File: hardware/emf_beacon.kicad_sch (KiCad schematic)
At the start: 4 parts

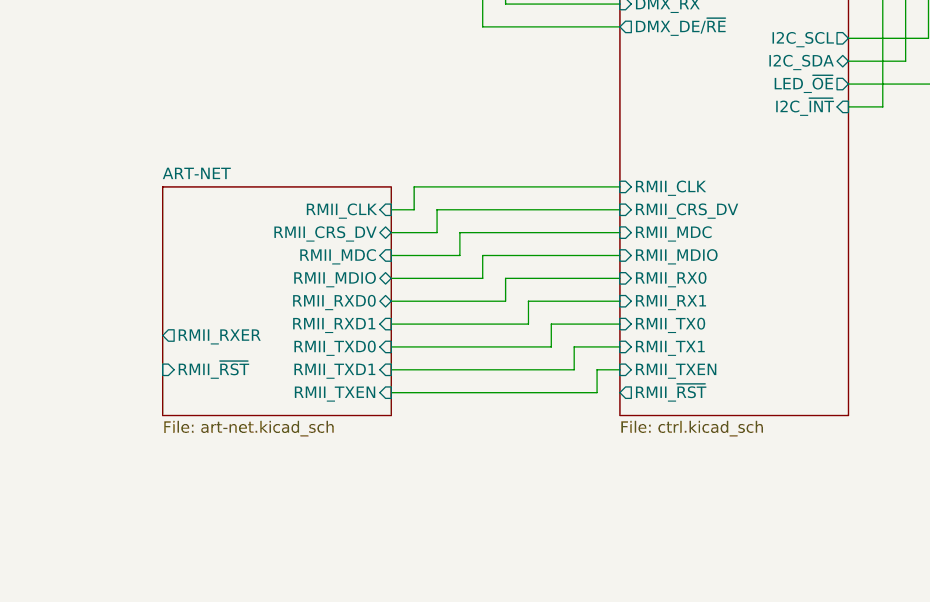
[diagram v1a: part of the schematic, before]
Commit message: removed Art-Net
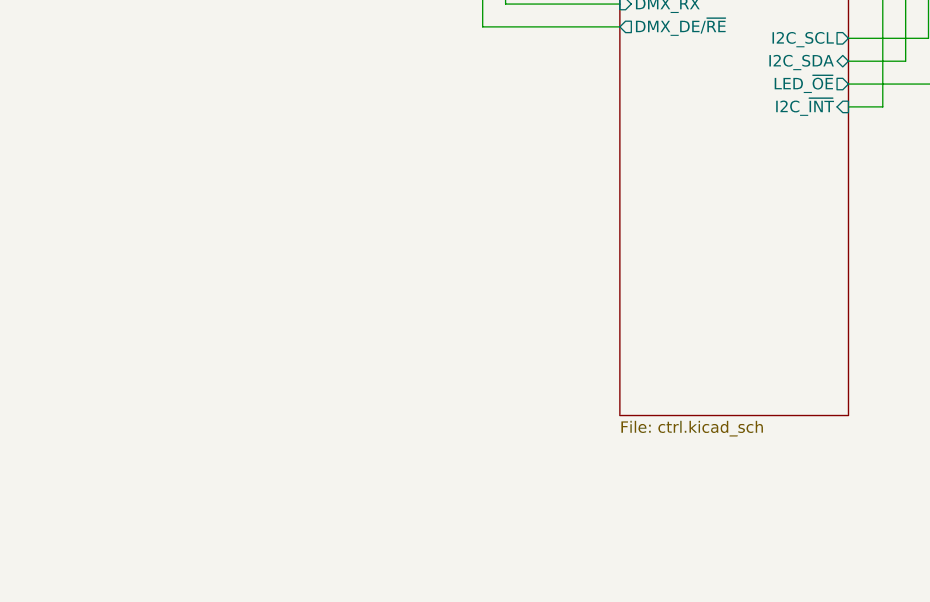
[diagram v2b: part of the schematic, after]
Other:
- removed sheet ART-NET
- sheet CTRL ports: added none; removed RMII_CLK, RMII_CRS_DV, RMII_MDC, RMII_MDIO, RMII_RX0, RMII_RX1, RMII_TX0, RMII_TX1, RMII_TXEN, RMII_~{RST}

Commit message: clean up
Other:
- note added: "LED Beacon"
- note removed: "DMX512's XLRs and Art-Net's RJ45 may get spun out to external PCBs"
- note removed: "Spec: Interfaces: Ideally DMX512 (5pin XLR) and Art-Net (RJ45) At least one, slight DMX512 preference +12V DC input weatherproof connections 10x 6.4V 0.3A LED strips Control: Treat as 10x lights per beacon be able to set normal brightness for each 'light' but fast enough for strobe effect for each 'light' Misc: JLC Assembly Target quantity is 15"

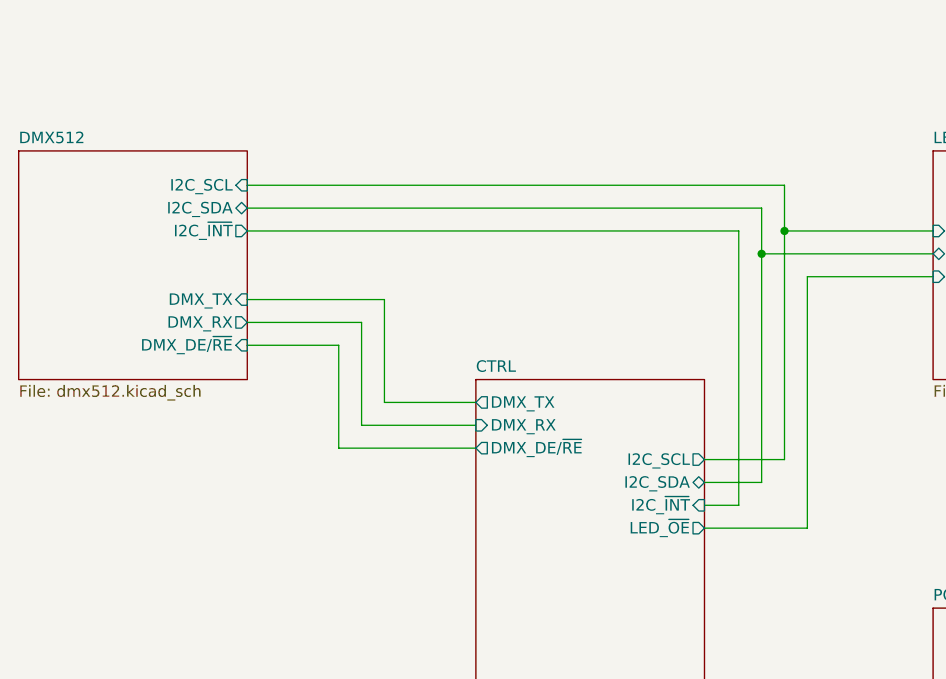
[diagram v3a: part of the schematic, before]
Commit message: adding snubbers, starting placement
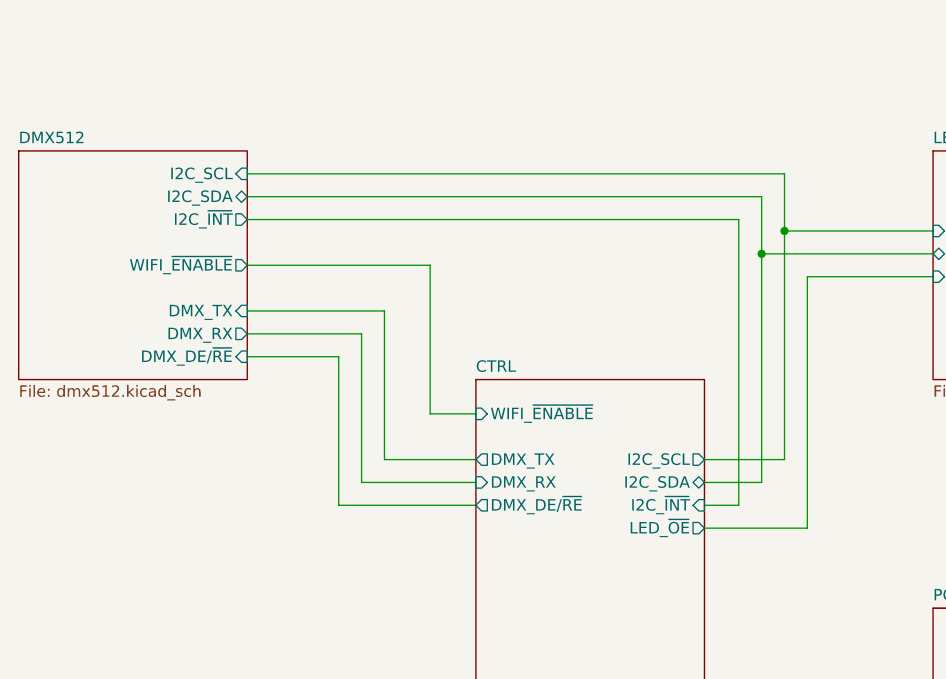
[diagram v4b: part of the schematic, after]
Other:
- sheet CTRL ports: added WIFI_~{ENABLE}; removed none
- sheet DMX512 ports: added WIFI_~{ENABLE}; removed none
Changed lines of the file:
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@@
 	(wire
 		(pts
-			(xy 116.84 78.74) (xy 127 78.74)
-		)
-		(stroke
-			(width 0)
-			(type default)
-		)
-	)
-	(wire
-		(pts
-			(xy 101.6 59.69) (xy 156.21 59.69)
-		)
-		(stroke
-			(width 0)
-			(type default)
-		)
-	)
-	(wire
-		(pts
-			(xy 156.21 59.69) (xy 156.21 90.17)
-		)
-		(stroke
-			(width 0)
-			(type default)
-		)
-	)
-	(wire
-		(pts
-			(xy 101.6 72.39) (xy 111.76 72.39)
-		)
-		(stroke
-			(width 0)
-			(type default)
-		)
-	)
-	(wire
-		(pts
-			(xy 101.6 57.15) (xy 158.75 57.15)
-		)
-		(stroke
-			(width 0)
-			(type default)
-		)
-	)
-	(wire
-		(pts
-			(xy 101.6 54.61) (xy 161.29 54.61)
+			(xy 116.84 85.09) (xy 127 85.09)
+		)
+		(stroke
+			(width 0)
+			(type default)
+		)
+	)
+	(wire
+		(pts
+			(xy 101.6 58.42) (xy 156.21 58.42)
+		)
+		(stroke
+			(width 0)
+			(type default)
+		)
+	)
+	(wire
+		(pts
+			(xy 156.21 58.42) (xy 156.21 90.17)
+		)
+		(stroke
+			(width 0)
+			(type default)
+		)
+	)
+	(wire
+		(pts
+			(xy 101.6 73.66) (xy 111.76 73.66)
+		)
+		(stroke
+			(width 0)
+			(type default)
+		)
+	)
+	(wire
+		(pts
+			(xy 101.6 55.88) (xy 158.75 55.88)
+		)
+		(stroke
+			(width 0)
+			(type default)
+		)
+	)
+	(wire
+		(pts
+			(xy 101.6 53.34) (xy 161.29 53.34)
 		)
 		(stroke
@@
 	(wire
 		(pts
-			(xy 127 81.28) (xy 114.3 81.28)
-		)
-		(stroke
-			(width 0)
-			(type default)
-		)
-	)
-	(wire
-		(pts
-			(xy 161.29 54.61) (xy 161.29 59.69)
+			(xy 127 87.63) (xy 114.3 87.63)
+		)
+		(stroke
+			(width 0)
+			(type default)
+		)
+	)
+	(wire
+		(pts
+			(xy 161.29 53.34) (xy 161.29 59.69)
+		)
+		(stroke
+			(width 0)
+			(type default)
+		)
+	)
+	(wire
+		(pts
+			(xy 121.92 63.5) (xy 101.6 63.5)
 		)
 		(stroke
@@
 	(wire
 		(pts
-			(xy 111.76 72.39) (xy 111.76 83.82)
+			(xy 111.76 73.66) (xy 111.76 90.17)
 		)
 		(stroke
@@
 	(wire
 		(pts
-			(xy 114.3 81.28) (xy 114.3 69.85)
+			(xy 114.3 87.63) (xy 114.3 71.12)
 		)
 		(stroke
@@
 	(wire
 		(pts
-			(xy 116.84 67.31) (xy 116.84 78.74)
+			(xy 121.92 80.01) (xy 121.92 63.5)
+		)
+		(stroke
+			(width 0)
+			(type default)
+		)
+	)
+	(wire
+		(pts
+			(xy 116.84 68.58) (xy 116.84 85.09)
 		)
 		(stroke
@@
 	(wire
 		(pts
-			(xy 158.75 57.15) (xy 158.75 62.23)
+			(xy 158.75 55.88) (xy 158.75 62.23)
 		)
 		(stroke
@@
 	(wire
 		(pts
-			(xy 111.76 83.82) (xy 127 83.82)
-		)
-		(stroke
-			(width 0)
-			(type default)
-		)
-	)
-	(wire
-		(pts
-			(xy 114.3 69.85) (xy 101.6 69.85)
-		)
-		(stroke
-			(width 0)
-			(type default)
-		)
-	)
-	(wire
-		(pts
-			(xy 101.6 67.31) (xy 116.84 67.31)
+			(xy 127 80.01) (xy 121.92 80.01)
+		)
+		(stroke
+			(width 0)
+			(type default)
+		)
+	)
+	(wire
+		(pts
+			(xy 111.76 90.17) (xy 127 90.17)
+		)
+		(stroke
+			(width 0)
+			(type default)
+		)
+	)
+	(wire
+		(pts
+			(xy 114.3 71.12) (xy 101.6 71.12)
+		)
+		(stroke
+			(width 0)
+			(type default)
+		)
+	)
+	(wire
+		(pts
+			(xy 101.6 68.58) (xy 116.84 68.58)
 		)
 		(stroke
@@
 		)
 		(pin "DMX_DE{slash}~{RE}" output
-			(at 127 83.82 180)
+			(at 127 90.17 180)
 			(effects
 				(font
@@
 		)
 		(pin "DMX_RX" input
-			(at 127 81.28 180)
+			(at 127 87.63 180)
 			(effects
 				(font
@@
 		)
 		(pin "DMX_TX" output
-			(at 127 78.74 180)
+			(at 127 85.09 180)
 			(effects
 				(font
@@
 				)
 				(justify right)
+			)
+		)
+		(pin "WIFI_~{ENABLE}" input
+			(at 127 80.01 180)
+			(effects
+				(font
+					(size 1.27 1.27)
+				)
+				(justify left)
 			)
 		)
@@
 		)
 		(pin "DMX_DE{slash}~{RE}" input
-			(at 101.6 72.39 0)
+			(at 101.6 73.66 0)
 			(effects
 				(font
@@
 		)
 		(pin "DMX_RX" output
-			(at 101.6 69.85 0)
+			(at 101.6 71.12 0)
 			(effects
 				(font
@@
 		)
 		(pin "DMX_TX" input
-			(at 101.6 67.31 0)
+			(at 101.6 68.58 0)
 			(effects
 				(font
@@
 		)
 		(pin "I2C_SDA" bidirectional
-			(at 101.6 57.15 0)
+			(at 101.6 55.88 0)
 			(effects
 				(font
@@
 		)
 		(pin "I2C_~{INT}" output
-			(at 101.6 59.69 0)
+			(at 101.6 58.42 0)
 			(effects
 				(font
@@
 		)
 		(pin "I2C_SCL" input
-			(at 101.6 54.61 0)
-			(effects
-				(font
+			(at 101.6 53.34 0)
+			(effects
+				(font
+					(size 1.27 1.27)
+				)
+				(justify right)
+			)
+		)
+		(pin "WIFI_~{ENABLE}" output
+			(at 101.6 63.5 0)
+			(effects
+				(font

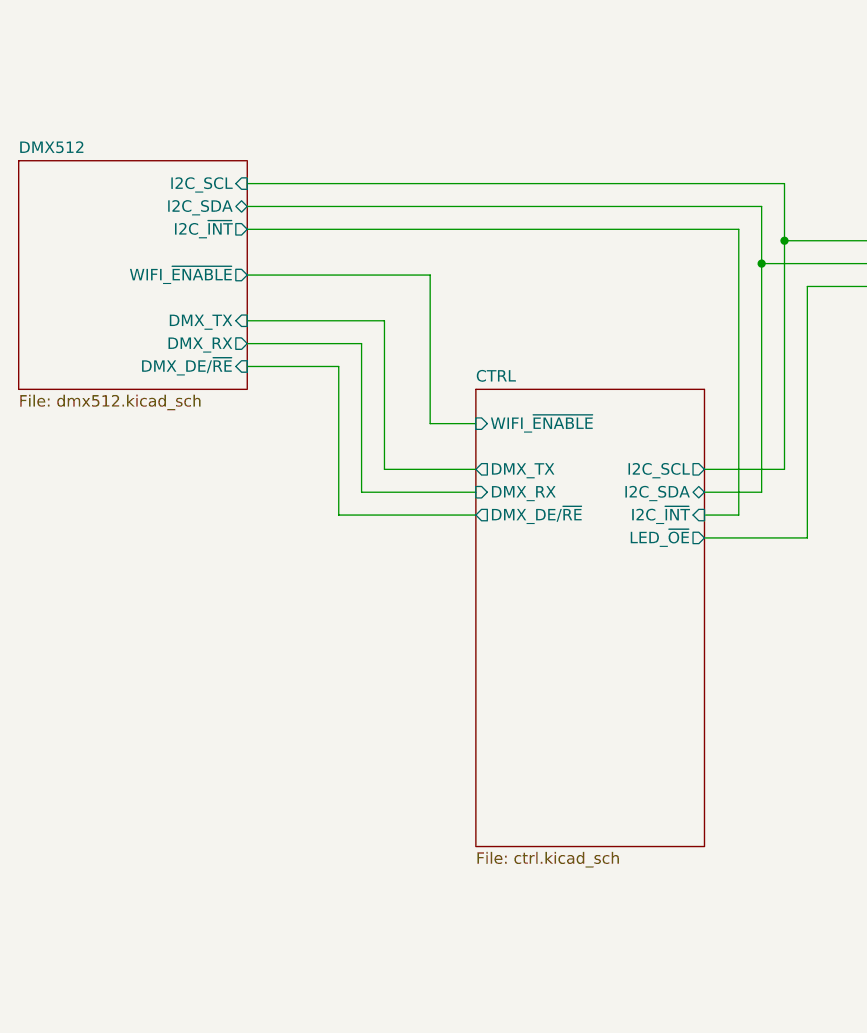
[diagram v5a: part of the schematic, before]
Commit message: sorting button and LED
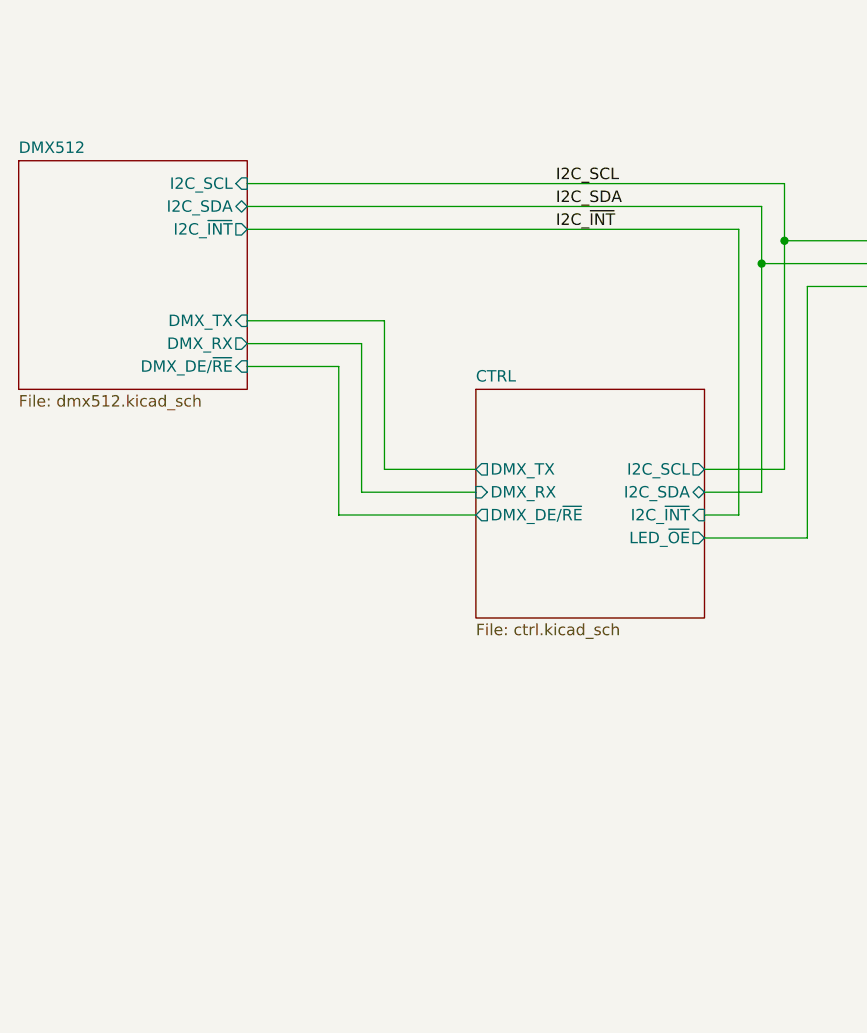
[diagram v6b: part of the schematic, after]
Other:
- sheet CTRL ports: added none; removed WIFI_~{ENABLE}
- sheet DMX512 ports: added none; removed WIFI_~{ENABLE}
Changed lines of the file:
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@@
-	(wire
-		(pts
-			(xy 121.92 63.5) (xy 101.6 63.5)
-		)
-		(stroke
-			(width 0)
-			(type default)
-		)
-	)
 	(wire
 		(pts
@@
 	(wire
 		(pts
-			(xy 121.92 80.01) (xy 121.92 63.5)
-		)
-		(stroke
-			(width 0)
-			(type default)
-		)
-	)
-	(wire
-		(pts
 			(xy 116.84 68.58) (xy 116.84 85.09)
 		)
@@
 	(wire
 		(pts
-			(xy 127 80.01) (xy 121.92 80.01)
-		)
-		(stroke
-			(width 0)
-			(type default)
-		)
-	)
-	(wire
-		(pts
 			(xy 111.76 90.17) (xy 127 90.17)
 		)
@@
 			(width 0)
 			(type default)
+		)
+	)
+	(label "I2C_~{INT}"
+		(at 135.89 58.42 0)
+		(effects
+			(font
+				(size 1.27 1.27)
+			)
+			(justify left bottom)
+		)
+	)
+	(label "I2C_SCL"
+		(at 135.89 53.34 0)
+		(effects
+			(font
+				(size 1.27 1.27)
+			)
+			(justify left bottom)
+		)
+	)
+	(label "I2C_SDA"
+		(at 135.89 55.88 0)
+		(effects
+			(font
+				(size 1.27 1.27)
+			)
+			(justify left bottom)
 		)
 	)
@@
 			)
 		)
-		(property "Rotation_offset" ""
-			(at 172.72 184.15 0)
-			(effects
-				(font
-					(size 1.27 1.27)
-				)
-				(hide yes)
-			)
-		)
 		(instances
 			(project "home_emf_beacon"
@@
 			)
 		)
-		(property "Rotation_offset" ""
-			(at 172.72 171.45 0)
-			(effects
-				(font
-					(size 1.27 1.27)
-				)
-				(hide yes)
-			)
-		)
 		(instances
 			(project ""
@@
 			)
 		)
-		(property "Rotation_offset" ""
-			(at 172.72 177.8 0)
-			(effects
-				(font
-					(size 1.27 1.27)
-				)
-				(hide yes)
-			)
-		)
 		(instances
 			(project "home_emf_beacon"
@@
 			)
 		)
-		(property "Rotation_offset" ""
-			(at 172.72 190.5 0)
-			(effects
-				(font
-					(size 1.27 1.27)
-				)
-				(hide yes)
-			)
-		)
 		(instances
 			(project "home_emf_beacon"
@@
 	(sheet
 		(at 127 76.2)
-		(size 25.4 50.8)
+		(size 25.4 25.4)
 		(exclude_from_sim no)
 		(in_bom yes)
@@
 		)
 		(property "Sheetfile" "ctrl.kicad_sch"
-			(at 127 127.5846 0)
+			(at 127 102.1846 0)
 			(effects
 				(font
@@
 				)
 				(justify right)
-			)
-		)
-		(pin "WIFI_~{ENABLE}" input
-			(at 127 80.01 180)
-			(effects
-				(font
-					(size 1.27 1.27)
-				)
-				(justify left)
 			)
 		)
@@
 			(effects
 				(font
-					(size 1.27 1.27)
-				)
-				(justify right)
-			)
-		)
-		(pin "WIFI_~{ENABLE}" output
-			(at 101.6 63.5 0)
-			(effects
-				(font

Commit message: starting layout
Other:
- sheet CTRL ports: added LED_~{PGD}; removed none
- sheet POWER ports: added LED_~{PGD}; removed none
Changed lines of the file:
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@@
+	(wire
+		(pts
+			(xy 163.83 114.3) (xy 163.83 95.25)
+		)
+		(stroke
+			(width 0)
+			(type default)
+		)
+	)
 	(wire
 		(pts
@@
 	(wire
 		(pts
+			(xy 177.8 114.3) (xy 163.83 114.3)
+		)
+		(stroke
+			(width 0)
+			(type default)
+		)
+	)
+	(wire
+		(pts
 			(xy 156.21 58.42) (xy 156.21 90.17)
 		)
@@
 		(pts
 			(xy 152.4 90.17) (xy 156.21 90.17)
+		)
+		(stroke
+			(width 0)
+			(type default)
+		)
+	)
+	(wire
+		(pts
+			(xy 152.4 95.25) (xy 163.83 95.25)
 		)
 		(stroke
@@
 			)
 		)
+		(pin "LED_~{PGD}" output
+			(at 177.8 114.3 180)
+			(effects
+				(font
+					(size 1.27 1.27)
+				)
+				(justify left)
+			)
+		)
 		(instances
 			(project "emf_beacon"
@@
 			(effects
 				(font
+					(size 1.27 1.27)
+				)
+				(justify right)
+			)
+		)
+		(pin "LED_~{PGD}" input
+			(at 152.4 95.25 0)
+			(effects
+				(font

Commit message: more layout and fixing OOS items
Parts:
- H1, H2, H3, H4: symbol Mechanical:MountingHole -> emf_beacon_ibrary:MountingHole
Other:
- sheet CTRL ports: added none; removed LED_~{PGD}
- sheet POWER ports: added none; removed LED_~{PGD}
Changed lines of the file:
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@@
-	(wire
-		(pts
-			(xy 163.83 114.3) (xy 163.83 95.25)
-		)
-		(stroke
-			(width 0)
-			(type default)
-		)
-	)
 	(wire
 		(pts
@@
 	(wire
 		(pts
-			(xy 177.8 114.3) (xy 163.83 114.3)
-		)
-		(stroke
-			(width 0)
-			(type default)
-		)
-	)
-	(wire
-		(pts
 			(xy 156.21 58.42) (xy 156.21 90.17)
 		)
@@
 		(pts
 			(xy 152.4 90.17) (xy 156.21 90.17)
-		)
-		(stroke
-			(width 0)
-			(type default)
-		)
-	)
-	(wire
-		(pts
-			(xy 152.4 95.25) (xy 163.83 95.25)
 		)
 		(stroke
@@
 	)
 	(symbol
-		(lib_id "Mechanical:MountingHole")
+		(lib_id "emf_beacon_ibrary:MountingHole")
 		(at 172.72 184.15 0)
 		(mirror y)
@@
 	)
 	(symbol
-		(lib_id "Mechanical:MountingHole")
+		(lib_id "emf_beacon_ibrary:MountingHole")
 		(at 172.72 171.45 0)
 		(mirror y)
@@
 	)
 	(symbol
-		(lib_id "Mechanical:MountingHole")
+		(lib_id "emf_beacon_ibrary:MountingHole")
 		(at 172.72 177.8 0)
 		(mirror y)
@@
 	)
 	(symbol
-		(lib_id "Mechanical:MountingHole")
+		(lib_id "emf_beacon_ibrary:MountingHole")
 		(at 172.72 190.5 0)
 		(mirror y)
@@
 			)
 		)
-		(pin "LED_~{PGD}" output
-			(at 177.8 114.3 180)
-			(effects
-				(font
-					(size 1.27 1.27)
-				)
-				(justify left)
-			)
-		)
 		(instances
 			(project "emf_beacon"
@@
 			(effects
 				(font
-					(size 1.27 1.27)
-				)
-				(justify right)
-			)
-		)
-		(pin "LED_~{PGD}" input
-			(at 152.4 95.25 0)
-			(effects
-				(font
